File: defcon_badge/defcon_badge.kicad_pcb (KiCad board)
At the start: 4 copper layers, 88 x 54 mm, 80 parts, among them J10 USB_C_Receptacle_GCT_USB4085, J11 JST-PH 2P, J20 AMPHENOL_10038075-D0P, J30 SAO 2x3, J31 microSD, J32 UART debug, J33 Dev/SWD header, SW1 SS-12D00, SW20 TS-1187A, SW21 TS-1187A, SW22 TS-1187A, U10 TP4056, U11 ME6211C33M5G, U2 W25Q16JVUXIQ, U20 TM8211, U21 TDA1308, U3 RP2040, U30 TSOP4838, Y1 ABM8-272-T3

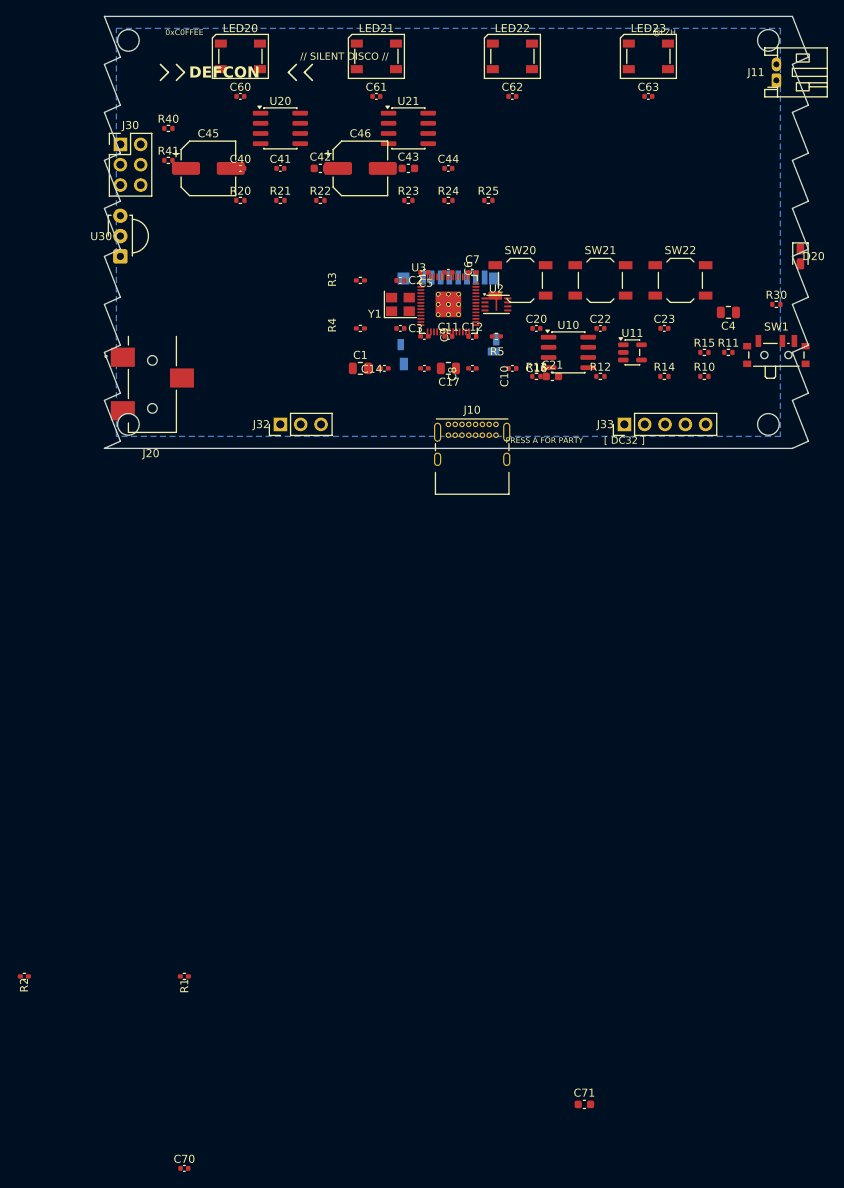
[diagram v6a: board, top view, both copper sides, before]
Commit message: iter(33): de-clutter pass — fix audio jack rotation, align buttons, regroup connectors
- J20 audio jack rotated 90° so plug exits UP off the top edge (was rot 180
  with body off in two directions). Top-right corner @ (174, 87).
- LEDs evenly spaced at 14mm pitch (116, 130, 144, 158)
- LED bypass caps aligned beneath at y=90
- Audio block: U20 + U21 at y=100 row, support caps at y=103, resistors at y=105
- 220u elcaps C45 + C46 spread apart (C45 at x=108, C46 at x=138)
- 3 buttons SW20-22 aligned in a row at y=98, x=155/165/175 (right side)
- Dev headers J33 SWD + J32 UART pulled OUT of the left edge (where they
  were colliding with U30 IR + J30 SAO + J33) and moved to right-side
  interior at x=170
- J30 SAO 2x3 at left edge interior y=119
- IR pair: U30 at left edge y=110 notch, D20 at right edge y=110 peak,
  C70/C71 + R1/R2 bypass and current-limit clustered around U30

Remaining minor overlaps (most <3mm²): J32↔J33 stacked vertically share
silk frame; J33↔U11 close; will fix in follow-up.

Co-Authored-By: Claude Opus 4.7 (1M context) <noreply@anthropic.com>
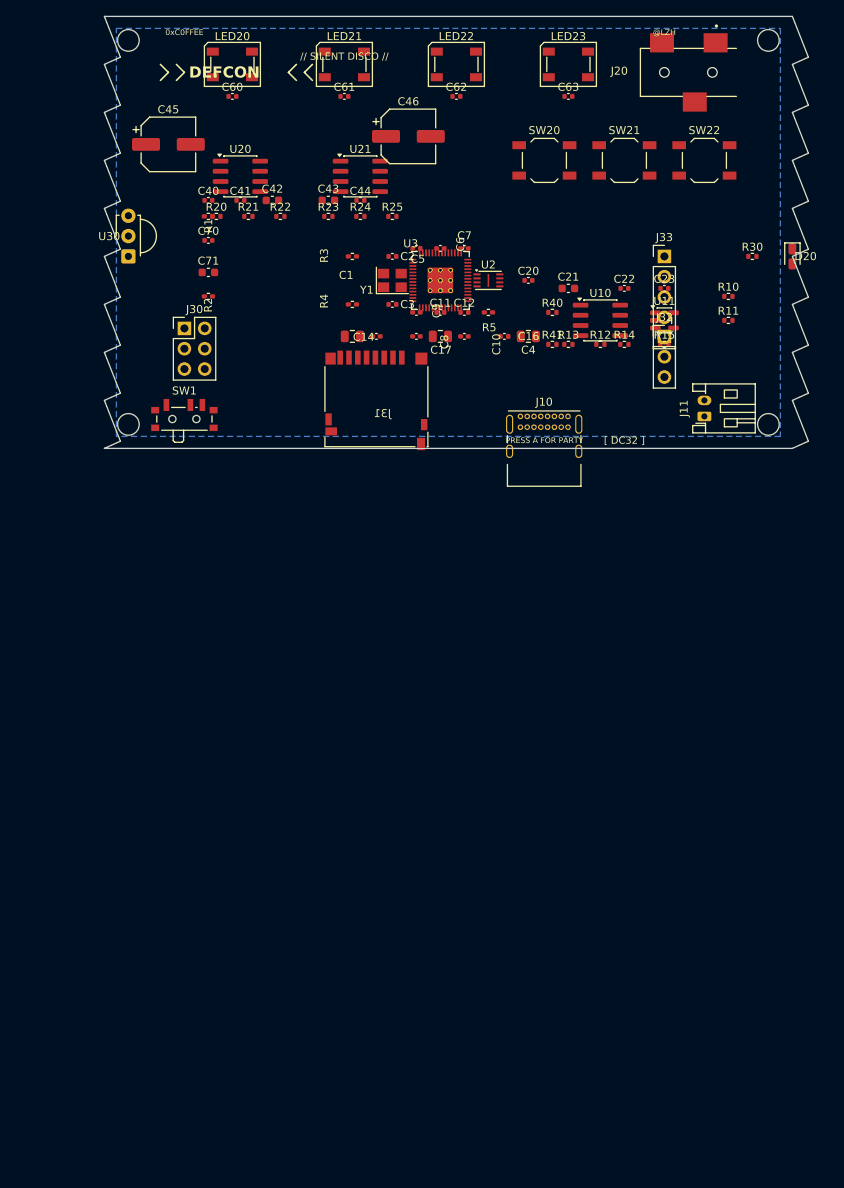
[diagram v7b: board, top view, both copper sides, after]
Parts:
- J31: moved to F.Cu
- moved C70 116.0 mm to (113.0, 108.0)
- moved C71 114.1 mm to (113.0, 112.0)
- moved R1 95.0 mm to (113.0, 105.0)
- moved R2 88.1 mm to (113.0, 115.0)
- moved J20 77.9 mm to (174.0, 87.0), turned to 90 degrees
- moved SW1 74.4 mm to (110.0, 130.0)
- moved R40 53.2 mm to (156.0, 117.0)
- moved R41 53.2 mm to (156.0, 121.0)
- moved J32 49.2 mm to (170.0, 120.0), turned to 0 degrees
- moved J11 43.0 mm to (175.0, 130.0)
- moved C4 25.2 mm to (153.0, 120.0)
- moved J30 24.4 mm to (110.0, 119.0)
- moved J33 21.6 mm to (170.0, 110.0), turned to 0 degrees
- moved SW20 15.3 mm to (155.0, 98.0)
- moved SW21 15.3 mm to (165.0, 98.0)
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
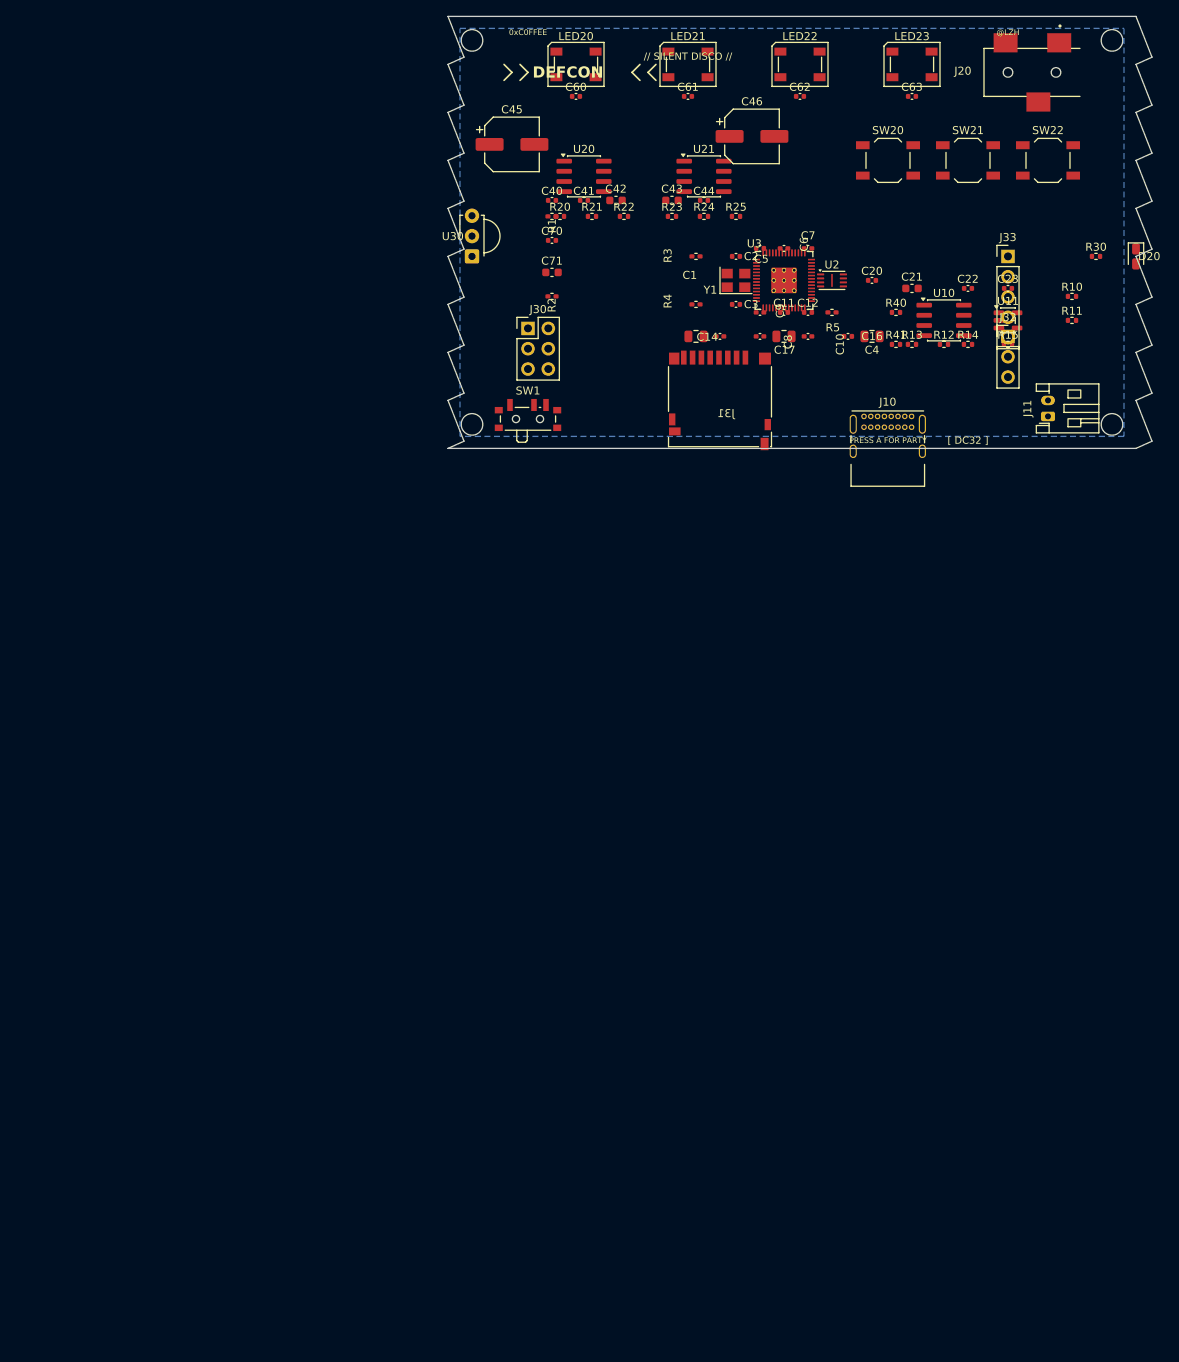
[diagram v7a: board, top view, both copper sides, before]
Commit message: iter(34): reset PCB to depopulated-sawtooth baseline (iter 30 redo state)
Restored defcon_badge.kicad_pcb from commit 19cb732 (real sawtooth +
all 76 components in staging grid at y≥200). Mounting holes remain at
the board corners.

Starting a methodical placement pass with the new pcb-placement tools:
fp_meta.py, render_area.py, place_at.py, align.py, ratsnest.py.

Co-Authored-By: Claude Opus 4.7 (1M context) <noreply@anthropic.com>
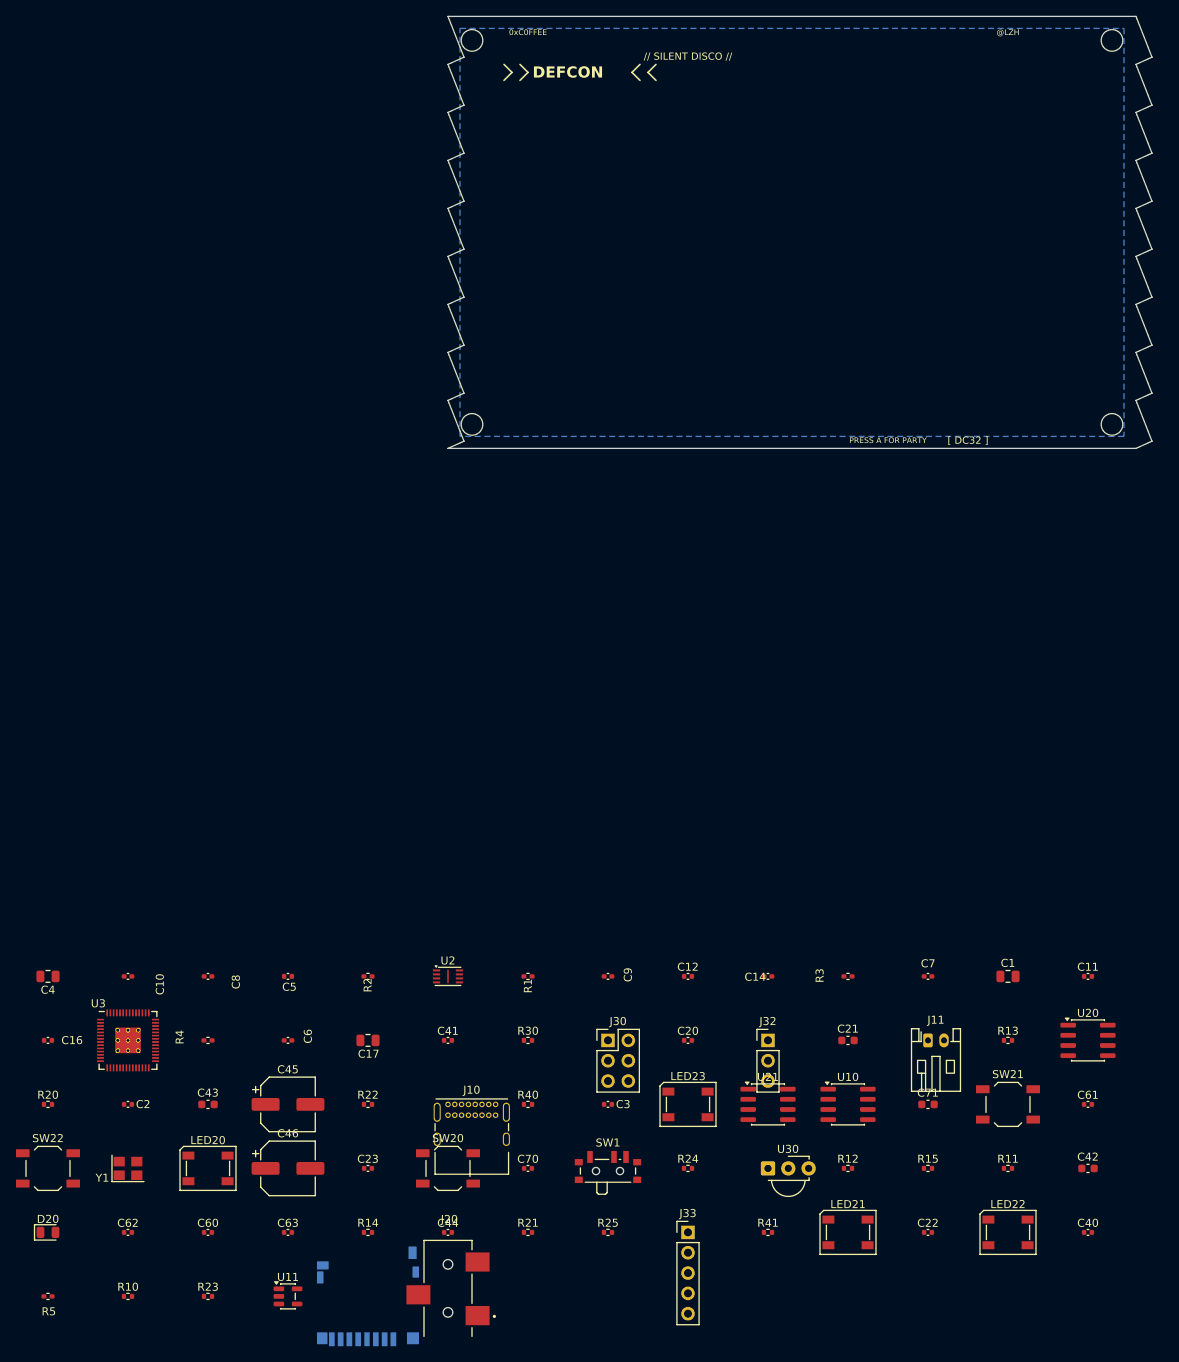
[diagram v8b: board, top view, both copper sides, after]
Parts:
- J31: moved to B.Cu
- moved D20 182.7 mm to (50.0, 232.0), turned to 0 degrees
- moved SW22 177.5 mm to (50.0, 224.0)
- moved R10 171.9 mm to (60.0, 240.0)
- moved J20 170.0 mm to (100.0, 240.0), turned to 0 degrees
- moved C62 165.0 mm to (60.0, 232.0)
- moved C63 162.0 mm to (80.0, 232.0)
- moved R5 157.3 mm to (50.0, 240.0)
- moved U11 151.6 mm to (80.0, 240.0)
- moved C60 149.3 mm to (70.0, 232.0)
- moved LED22 148.3 mm to (170.0, 232.0)
- moved LED21 147.4 mm to (150.0, 232.0)
- moved R23 146.9 mm to (70.0, 240.0)
- moved LED20 145.5 mm to (70.0, 224.0)
- moved C40 145.4 mm to (180.0, 232.0)
- moved C46 141.4 mm to (80.0, 224.0)
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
